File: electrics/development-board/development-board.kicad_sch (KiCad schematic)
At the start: 36 parts, among them J1 East, J10 Ext_5V, J8 West, J9 PinOut, Q3 S8050, Q4 S8050, SW1 Reset, SW2 Setup, SW3 Power, U1 LD1117S33

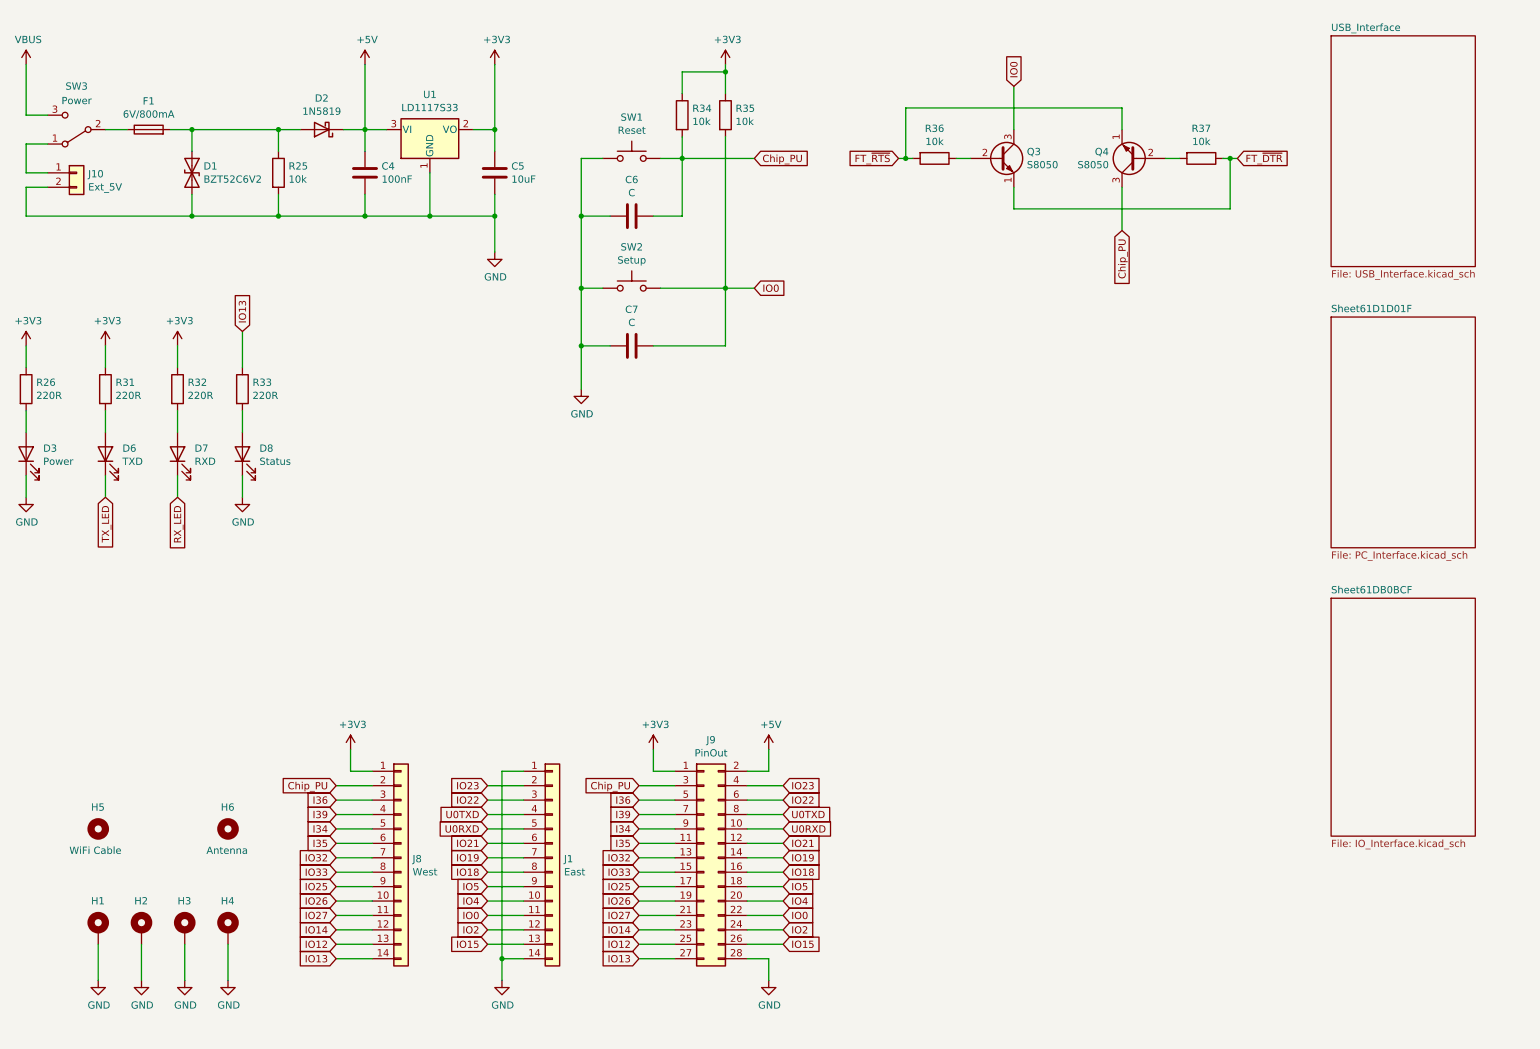
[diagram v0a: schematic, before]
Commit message: Fix all ERC and DRC warnings during build
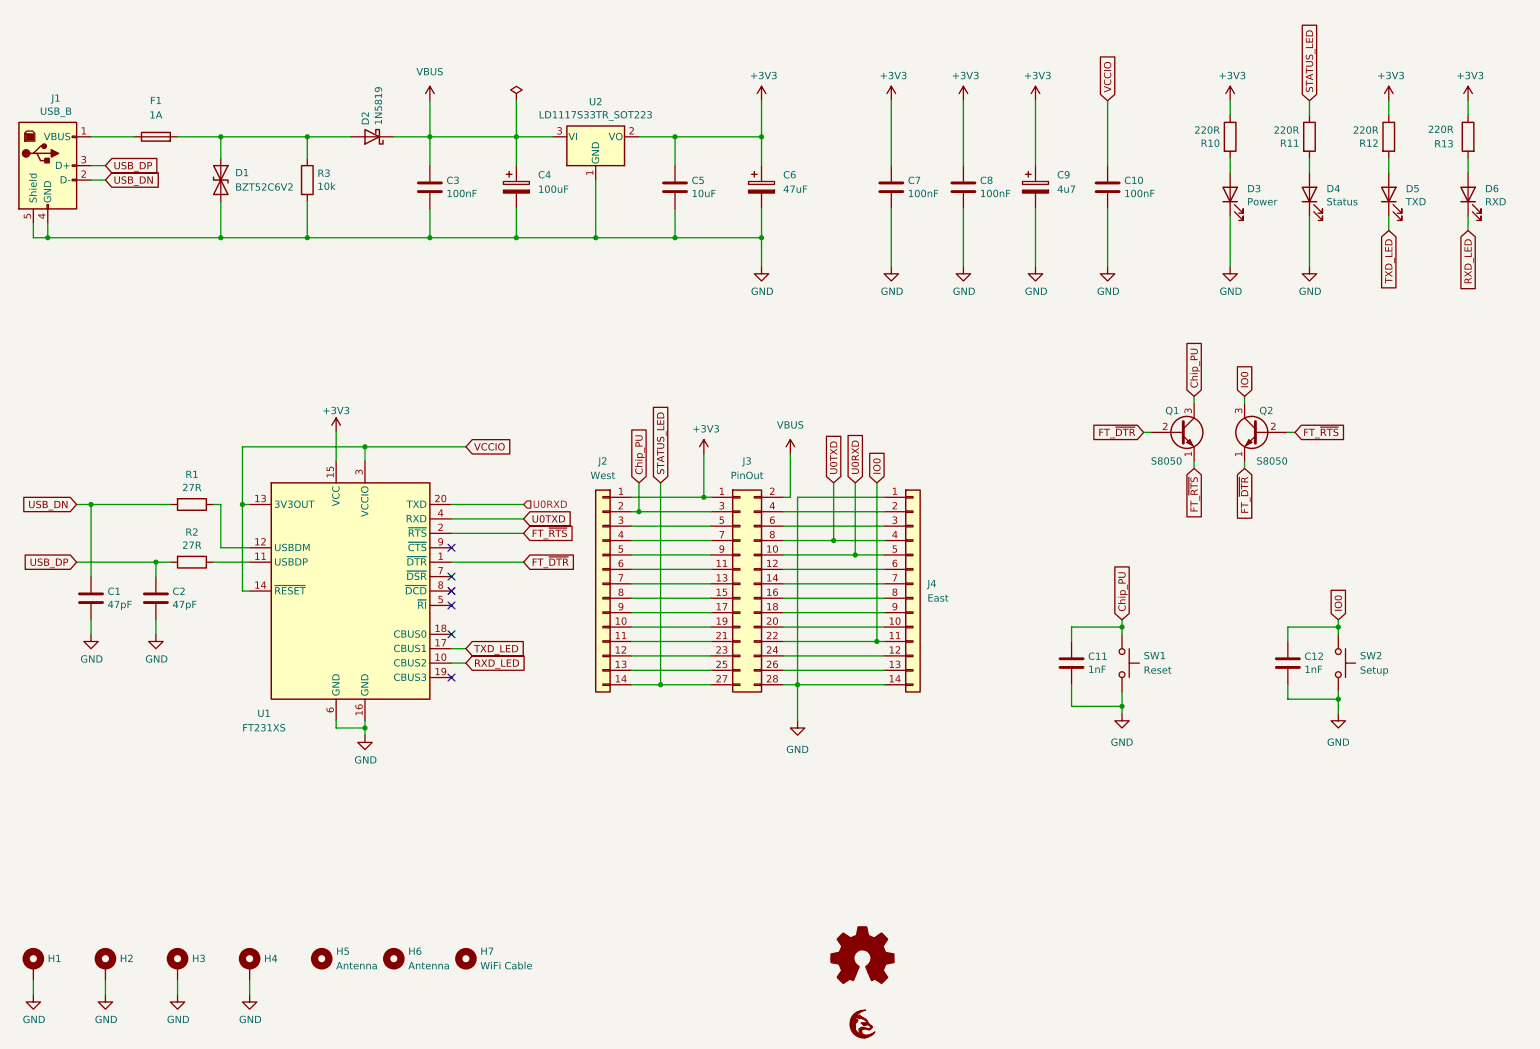
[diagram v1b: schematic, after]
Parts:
- removed C4: 100nF, Capacitor_SMD:C_1206_3216Metric_Pad1.33x1.80mm_HandSolder, symbol Device:C
- removed C6: C, Capacitor_SMD:C_1206_3216Metric_Pad1.33x1.80mm_HandSolder, symbol Device:C
- removed D7: RXD, LED_SMD:LED_1206_3216Metric_Pad1.42x1.75mm_HandSolder, symbol Device:LED
- removed D8: Status, LED_SMD:LED_1206_3216Metric_Pad1.42x1.75mm_HandSolder, symbol Device:LED
- removed J1: East, Connector_PinHeader_2.54mm:PinHeader_1x14_P2.54mm_Vertical, symbol Connector_Generic:Conn_01x14
- removed J10: Ext_5V, Connector_PinHeader_2.54mm:PinHeader_1x02_P2.54mm_Horizontal, symbol Connector_Generic:Conn_01x02
- removed J8: West, Connector_PinHeader_2.54mm:PinHeader_1x14_P2.54mm_Vertical, symbol Connector_Generic:Conn_01x14
- removed J9: PinOut, Connector_PinHeader_2.54mm:PinHeader_2x14_P2.54mm_Vertical, symbol Connector_Generic:Conn_02x14_Odd_Even
- removed Q3, Q4: S8050, Package_TO_SOT_SMD:SOT-23, symbol Transistor_BJT:S8050
- removed R25, R34, R35, R36, R37: 10k, Resistor_SMD:R_1206_3216Metric_Pad1.30x1.75mm_HandSolder, symbol Device:R
- removed R26, R31, R32, R33: 220R, Resistor_SMD:R_1206_3216Metric_Pad1.30x1.75mm_HandSolder, symbol Device:R
- removed SW3: Power, Button_Switch_THT:SW_E-Switch_EG1224_SPDT_Angled, symbol Switch:SW_SPDT
- removed U1: LD1117S33, Package_TO_SOT_SMD:SOT-223-3_TabPin2, symbol Regulator_Linear:LD1117S33TR_SOT223
- added C1, C2: 47pF, Capacitor_SMD:C_1206_3216Metric_Pad1.33x1.80mm_HandSolder, symbol Device:C
- added C10, C3, C8: 100nF, Capacitor_SMD:C_1206_3216Metric_Pad1.33x1.80mm_HandSolder, symbol Device:C
- added C11, C12: 1nF, Capacitor_SMD:C_1206_3216Metric_Pad1.33x1.80mm_HandSolder, symbol Device:C
- added C4: 100uF, Capacitor_SMD:CP_Elec_5x5.3, symbol Device:C_Polarized
- added C6: 47uF, Capacitor_SMD:CP_Elec_5x5.3, symbol Device:C_Polarized
- added C9: 4u7, Capacitor_Tantalum_SMD:CP_EIA-3216-18_Kemet-A_Pad1.58x1.35mm_HandSolder, symbol Device:C_Polarized
- added D4: Status, LED_SMD:LED_1206_3216Metric_Pad1.42x1.75mm_HandSolder, symbol Device:LED
- added D5: TXD, LED_SMD:LED_1206_3216Metric_Pad1.42x1.75mm_HandSolder, symbol Device:LED
- added H7: WiFi Cable, MountingHole:MountingHole_5.5mm, symbol Mechanical:MountingHole
- added J1: USB_B, Connector_USB:USB_B_OST_USB-B1HSxx_Horizontal, symbol Connector:USB_B
- added J2: West, Connector_PinHeader_2.54mm:PinHeader_1x14_P2.54mm_Vertical, symbol Connector_Generic:Conn_01x14
- added J3: PinOut, Connector_PinHeader_2.54mm:PinHeader_2x14_P2.54mm_Vertical, symbol Connector_Generic:Conn_02x14_Odd_Even
- added J4: East, Connector_PinHeader_2.54mm:PinHeader_1x14_P2.54mm_Vertical, symbol Connector_Generic:Conn_01x14
- added LOGO1: Logo_Open_Hardware_Small, Symbol:OSHW-Logo2_7.3x6mm_SilkScreen, symbol Graphic:Logo_Open_Hardware_Small
- added LOGO2: LOGO, images:grayc-logo-negative, symbol grayc-logo-negative:LOGO
- added Q1, Q2: S8050, Package_TO_SOT_SMD:SOT-23, symbol Transistor_BJT:S8050
- added R1, R2: 27R, Resistor_SMD:R_1206_3216Metric_Pad1.30x1.75mm_HandSolder, symbol Device:R
- added R10, R11, R12, R13: 220R, Resistor_SMD:R_1206_3216Metric_Pad1.30x1.75mm_HandSolder, symbol Device:R
- added R3: 10k, Resistor_SMD:R_1206_3216Metric_Pad1.30x1.75mm_HandSolder, symbol Device:R
- added U1: FT231XS, Package_SO:SSOP-20_3.9x8.7mm_P0.635mm, symbol Interface_USB:FT231XS
- added U2: LD1117S33TR_SOT223, Package_TO_SOT_SMD:SOT-223-3_TabPin2, symbol Regulator_Linear:LD1117S33TR_SOT223
- C5: #manf (none) -> LMK316BJ106KL-T
- C7: value C -> 100nF; #manf (none) -> TMF316B7104KLHT
- D1: #manf (none) -> BZT52-C6V2S_R1_00001
- D2: #manf (none) -> 1N5819HW-7-F
- D3: #manf (none) -> APT3216MGC
- D6: value TXD -> RXD; #manf (none) -> APT3216MGC
- F1: value 6V/800mA -> 1A; #manf (none) -> TR/3216FF1-R
- H1, H2, H3, H4, H6: now left out of the parts list
- H5: value WiFi Cable -> Antenna; now left out of the parts list
- SW1, SW2: #manf (none) -> PTS645SK43SMTR92LFS
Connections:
- net +5V is gone; now on net VBUS: D2.1 (K)
- net +3V3: now also C7.1, C6.1, C8.1, C9.1, J2.1 (Pin_1), J3.1 (Pin_1), R10.1, R12.1, R13.1, U1.15 (VCC), U2.2 (VO)
- net Chip_PU: now also C11.1, J2.2 (Pin_2), J3.3 (Pin_3), Q1.3 (C)
- net FT_~{DTR}: now also Q1.2 (B), Q2.1 (E), U1.1 (~{DTR})
- net FT_~{RTS}: now also Q1.1 (E), Q2.2 (B), U1.2 (~{RTS})
- net GND: now also C1.2, C10.2, C11.2, C12.2, C2.2, C3.2, C4.2, C6.2, C8.2, C9.2, D4.1 (K), J1.4 (GND), J1.5 (Shield), J3.28 (Pin_28), J4.1 (Pin_1), J4.14 (Pin_14), R3.2, U1.16 (GND), U1.6 (GND), U2.1 (GND)
- net IO0: now also C12.1, J3.22 (Pin_22), J4.11 (Pin_11), Q2.3 (C); no longer C7.1
- net U0RXD: now also J3.10 (Pin_10), J4.5 (Pin_5), U1.20 (TXD)
- net U0TXD: now also J3.8 (Pin_8), J4.4 (Pin_4), U1.4 (RXD)
- net VBUS: now also C3.1, C4.1, J3.2 (Pin_2), U2.3 (VI)
- net at D3.2 (A): now also R10.2
- net at D1.1 (A1), D2.2 (A), F1.2: now also R3.1
- net at F1.1: now also J1.1 (VBUS)
- net at D6.2 (A): now also R13.2
- net TX_LED renamed RXD_LED
- net RXD_LED: now also U1.10 (CBUS2)
- new net: D5.2 (A), R12.2
- new net: J2.10 (Pin_10), J3.19 (Pin_19)
- new net: J2.11 (Pin_11), J3.21 (Pin_21)
- new net: J2.12 (Pin_12), J3.23 (Pin_23)
- new net: J2.13 (Pin_13), J3.25 (Pin_25)
- new net: J2.3 (Pin_3), J3.5 (Pin_5)
- new net: J2.4 (Pin_4), J3.7 (Pin_7)
- new net: J2.5 (Pin_5), J3.9 (Pin_9)
- new net: J2.6 (Pin_6), J3.11 (Pin_11)
- new net: J2.7 (Pin_7), J3.13 (Pin_13)
- new net: J2.8 (Pin_8), J3.15 (Pin_15)
- new net: J2.9 (Pin_9), J3.17 (Pin_17)
- new net: D4.2 (A), R11.2
- new net: R2.1, U1.11 (USBDP)
- new net: R1.1, U1.12 (USBDM)
- new net: J3.12 (Pin_12), J4.6 (Pin_6)
- new net: J3.14 (Pin_14), J4.7 (Pin_7)
- new net: J3.16 (Pin_16), J4.8 (Pin_8)
- new net: J3.18 (Pin_18), J4.9 (Pin_9)
- new net: J3.20 (Pin_20), J4.10 (Pin_10)
- new net: J3.24 (Pin_24), J4.12 (Pin_12)
- new net: J3.26 (Pin_26), J4.13 (Pin_13)
- new net: J3.4 (Pin_4), J4.2 (Pin_2)
- new net: J3.6 (Pin_6), J4.3 (Pin_3)
- new net STATUS_LED: J2.14 (Pin_14), J3.27 (Pin_27), R11.1
- new net TXD_LED: D5.1 (K), U1.17 (CBUS1)
- new net USB_DN: C1.1, J1.2 (D-), R1.2
- new net USB_DP: C2.1, J1.3 (D+), R2.2
- new net VCCIO: C10.1, U1.13 (3V3OUT), U1.14 (~{RESET}), U1.3 (VCCIO)
- no-connect marks 0 -> 6
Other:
- removed sheet Sheet61D1D01F
- removed sheet Sheet61DB0BCF
- removed sheet USB_Interface
- company: (none) -> GrayC GmbH
- title: (none) -> Satellite Development Board
